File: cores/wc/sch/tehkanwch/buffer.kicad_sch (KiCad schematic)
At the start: 11 parts

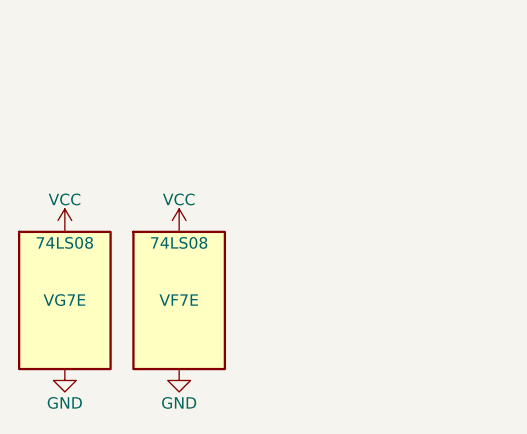
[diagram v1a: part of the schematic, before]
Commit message: wc: support for analog gamepad
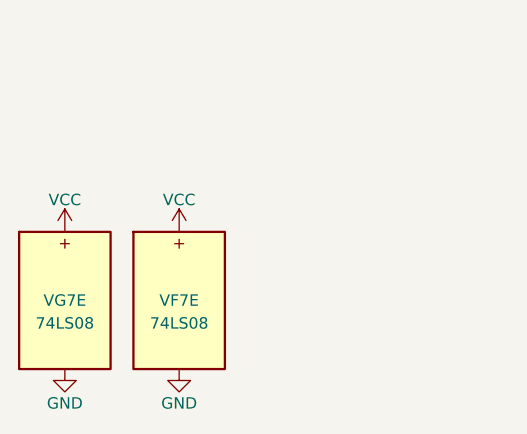
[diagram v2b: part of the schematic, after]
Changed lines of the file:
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@@
 		)
 		(property "Value" "74LS08"
-			(at 38.0917 259.08 0)
+			(at 38.1 267.97 0)
 			(effects
 				(font
@@
 		)
 		(property "Value" "74LS08"
-			(at 25.3917 259.08 0)
-			(effects
-				(font
+			(at 25.4 267.97 0)
+			(effects
+				(font
